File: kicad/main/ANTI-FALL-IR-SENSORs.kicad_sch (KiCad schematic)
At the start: 11 parts, among them Q5 2302V, Q6 2302V

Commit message: Second review round
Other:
- note removed: "L1- R4 L4 LR? LF? RF? RR? LR-"
- note removed: "R2+ R3 L3 LR? LF? RF? RR? RR+"
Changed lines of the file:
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@@
 	(generator_version "10.0")
 	(paper "A2")
-	(rectangle
-		(start 244.348 178.308)
-		(end 351.536 279.908)
-		(stroke
-			(width 0)
-			(type solid)
-		)
-		(fill
-			(type color)
-			(color 72 0 0 1)
-		)
-	)
-	(text "L1-\nR4\nL4\nLR?\nLF?\nRF?\nRR?\nLR-"
-		(exclude_from_sim no)
-		(at 290.322 202.946 0)
-		(effects
-			(font
-				(size 1.5748 1.5748)
-			)
-			(justify left)
-		)
-	)
 	(text "ANTI FALL SENSORs"
 		(exclude_from_sim no)
@@
 		)
 	)
-	(text "R2+\nR3\nL3\nLR?\nLF?\nRF?\nRR?\nRR+"
-		(exclude_from_sim no)
-		(at 312.928 202.946 0)
-		(effects
-			(font
-				(size 1.5748 1.5748)
-			)
-			(justify left)
-		)
-	)

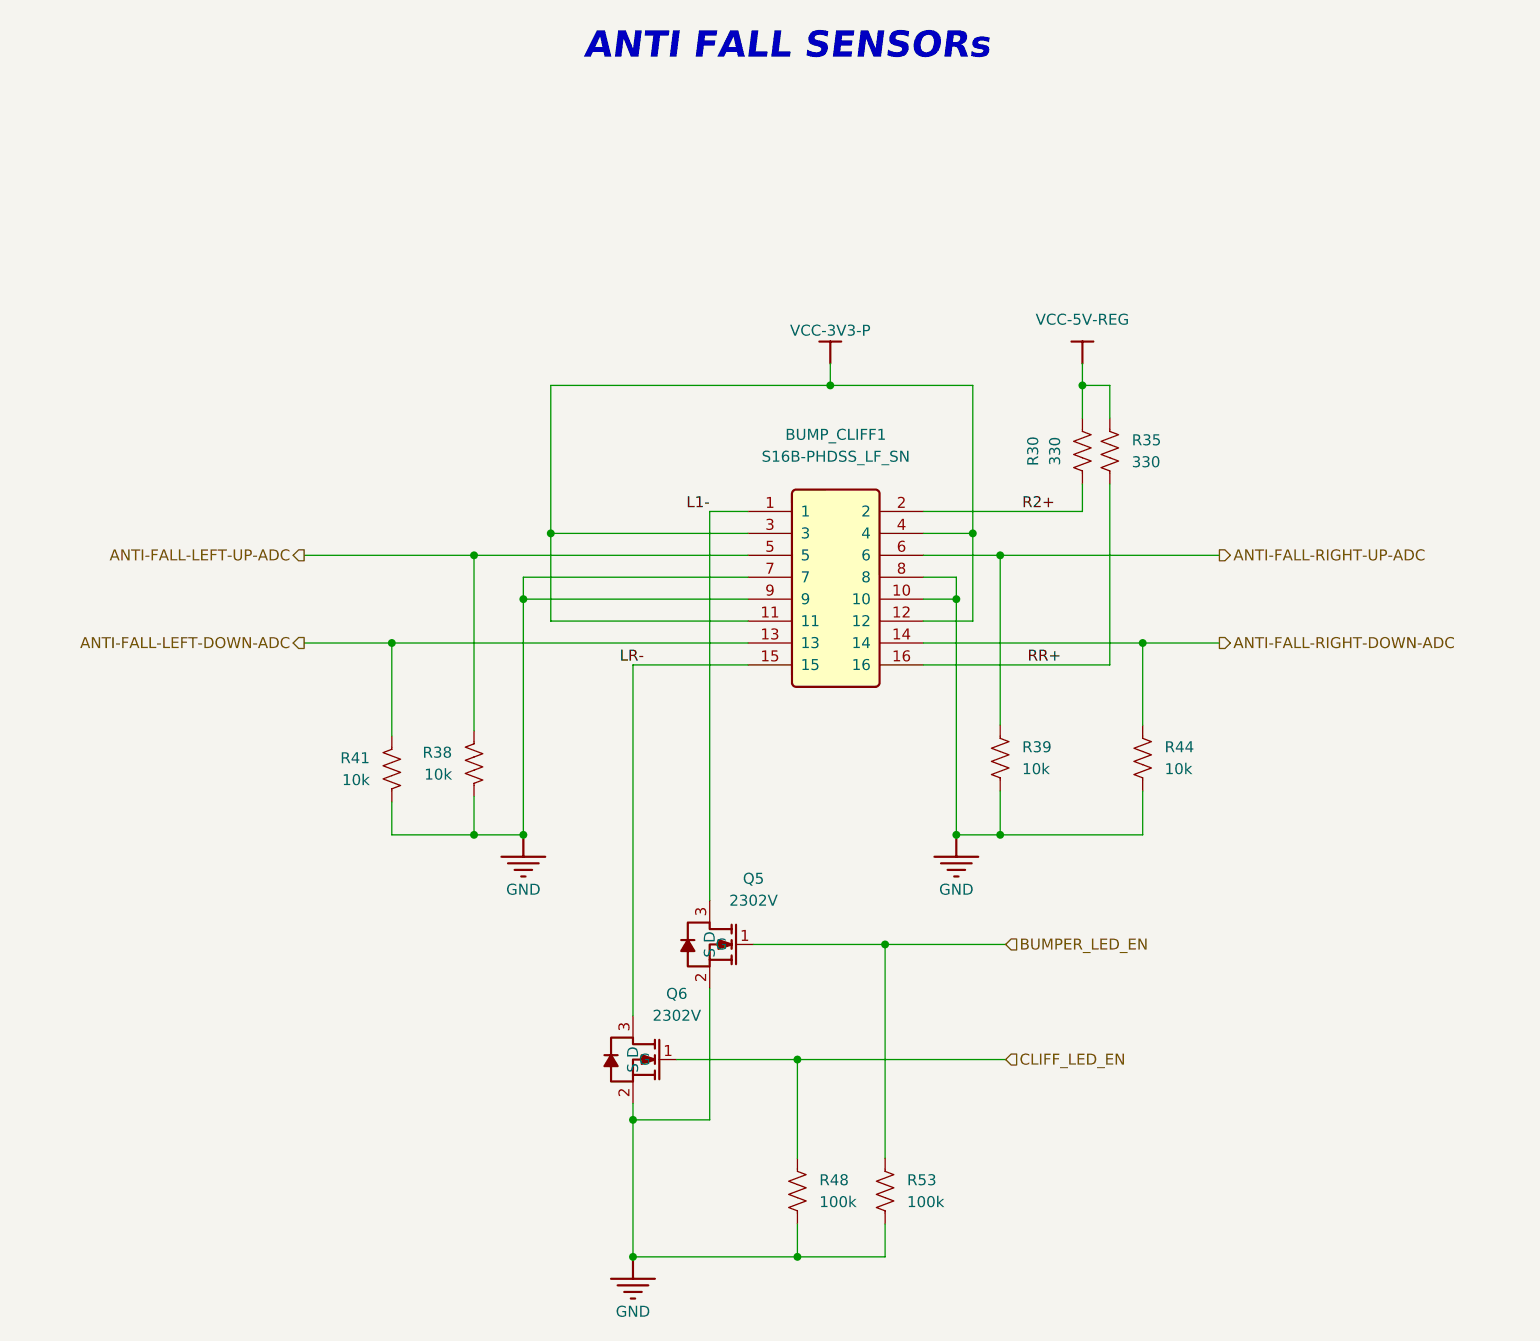
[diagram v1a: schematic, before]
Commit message: Cliff/bumpers connector
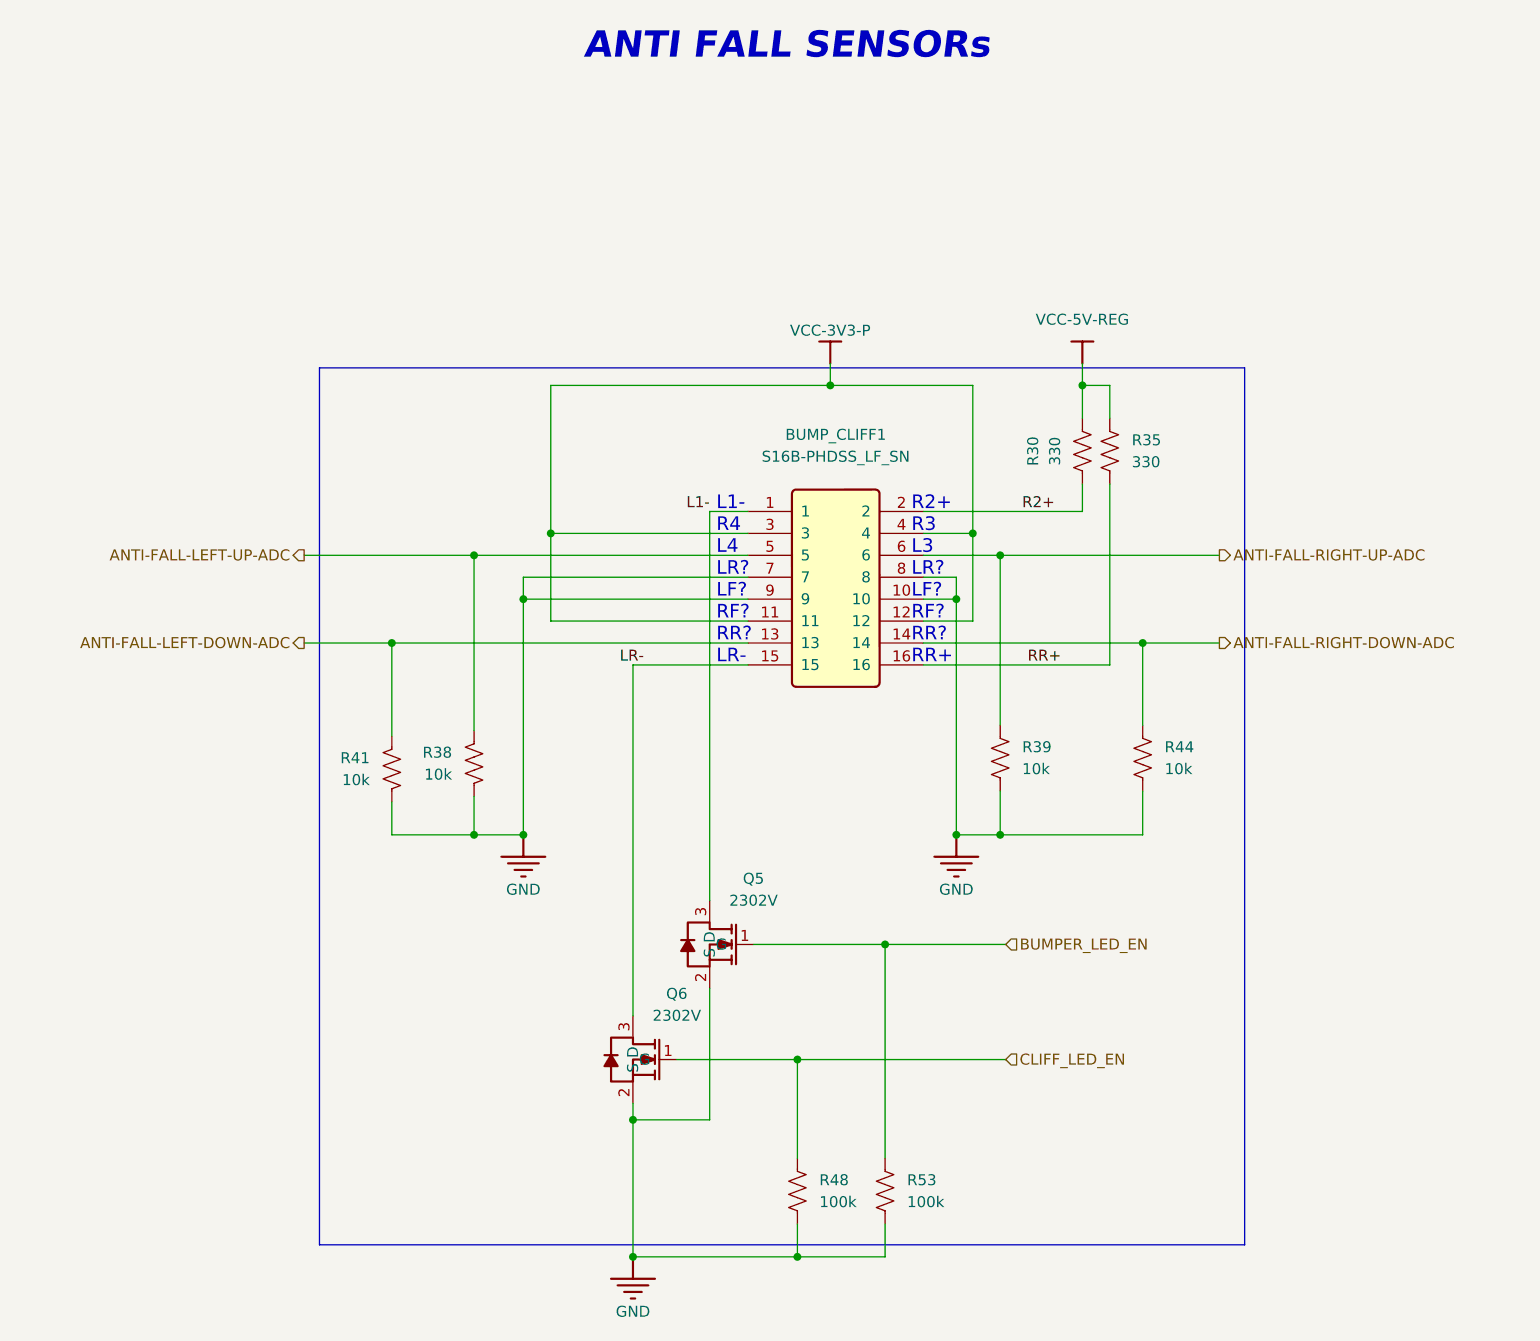
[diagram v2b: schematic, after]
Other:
- note added: "L1- R4 L4 LR? LF? RF? RR? LR-"
- note added: "R2+ R3 L3 LR? LF? RF? RR? RR+"
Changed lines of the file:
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@@
 	(generator_version "10.0")
 	(paper "A2")
+	(rectangle
+		(start 244.348 178.308)
+		(end 351.536 279.908)
+		(stroke
+			(width 0)
+			(type solid)
+		)
+		(fill
+			(type color)
+			(color 72 0 0 1)
+		)
+	)
+	(text "L1-\nR4\nL4\nLR?\nLF?\nRF?\nRR?\nLR-"
+		(exclude_from_sim no)
+		(at 290.322 202.946 0)
+		(effects
+			(font
+				(size 1.5748 1.5748)
+			)
+			(justify left)
+		)
+	)
 	(text "ANTI FALL SENSORs"
 		(exclude_from_sim no)
@@
 		)
 	)
+	(text "R2+\nR3\nL3\nLR?\nLF?\nRF?\nRR?\nRR+"
+		(exclude_from_sim no)
+		(at 312.928 202.946 0)
+		(effects
+			(font
+				(size 1.5748 1.5748)
+			)
+			(justify left)
+		)
+	)
